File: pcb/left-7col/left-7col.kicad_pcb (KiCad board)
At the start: 2 copper layers, 126 x 92 mm, 54 parts, among them SW1 SW_SPDT_312, SW2 SW_SPST, U1 SuperMini

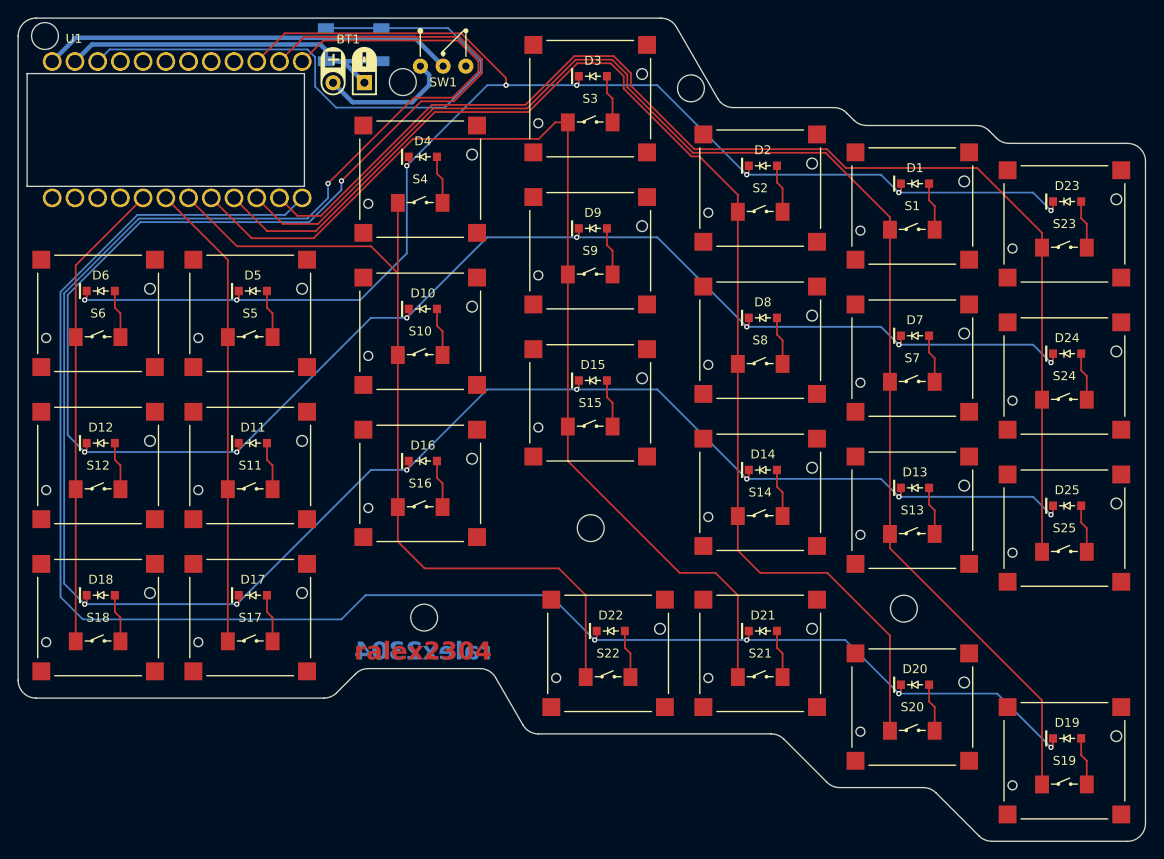
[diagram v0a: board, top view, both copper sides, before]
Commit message: Change horizontal spacing and add nice!view to left half
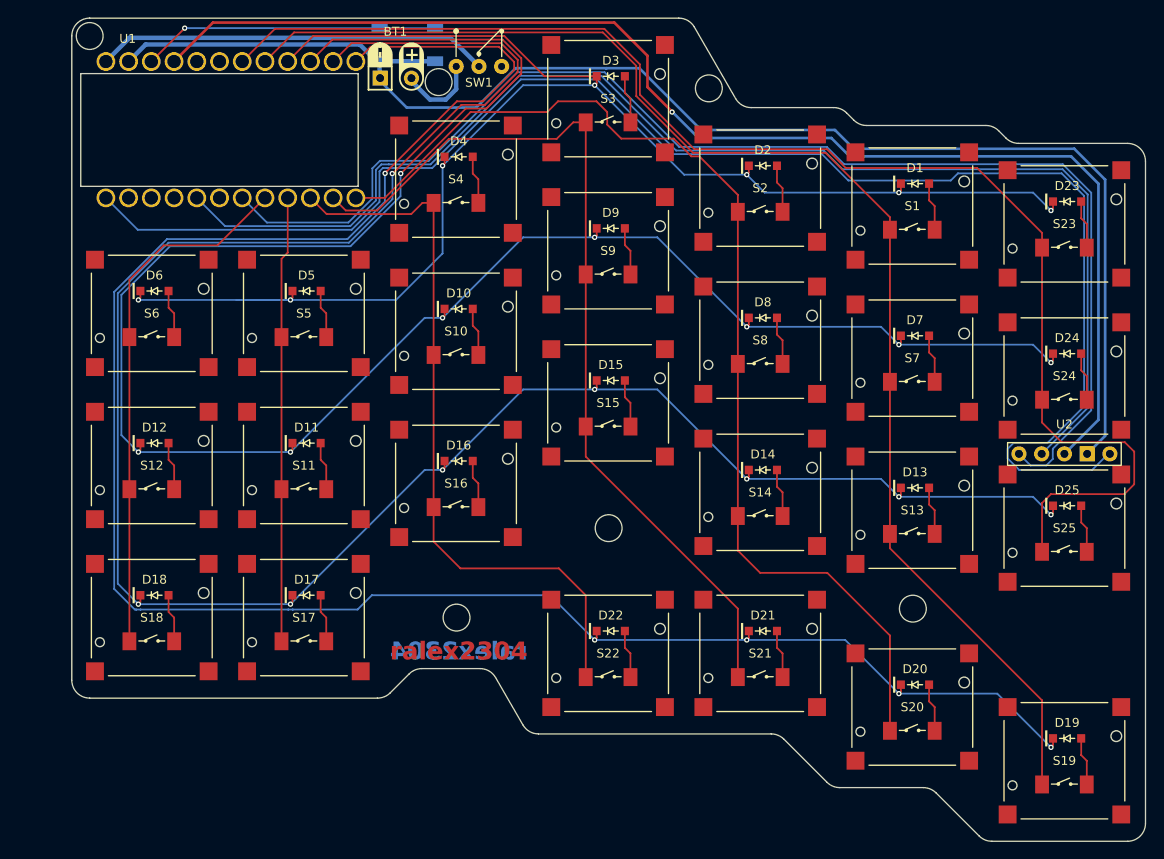
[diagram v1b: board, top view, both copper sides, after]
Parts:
- added U2: nice!view, strizh_lib:nice_view, F.Cu at (197.0, 109.0)
- moved D11 6.00 mm to (112.3, 106.5)
- moved D12 6.00 mm to (95.3, 106.5)
- moved D17 6.00 mm to (112.3, 123.5)
- moved D18 6.00 mm to (95.3, 123.5)
- moved D5 6.00 mm to (112.3, 89.5)
- moved D6 6.00 mm to (95.3, 89.5)
- moved S11 6.00 mm to (112.0, 109.0)
- moved S12 6.00 mm to (95.0, 109.0)
- moved S17 6.00 mm to (112.0, 126.0)
- moved S18 6.00 mm to (95.0, 126.0)
- moved S5 6.00 mm to (112.0, 92.0)
- moved S6 6.00 mm to (95.0, 92.0)
- moved SW2 6.00 mm to (123.6, 62.0)
- moved U1 6.00 mm to (84.8, 71.5)
- moved BT1 5.19 mm to (122.1, 64.5)
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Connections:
- U1 pad 1: unconnected-(U1-TX/D0/006-Pad1) -> cs
- U1 pad 10: COL6 -> COL3
- U1 pad 11: COL7 -> COL4
- U1 pad 12: ROW4 -> COL5
- U1 pad 13: ROW3 -> ROW4
- U1 pad 14: ROW2 -> ROW3
- U1 pad 15: ROW1 -> ROW2
- U1 pad 16: unconnected-(U1-SDA1/D13/113-Pad16) -> ROW1
- U1 pad 17: unconnected-(U1-SCL1/D14/115-Pad17) -> COL6
- U1 pad 18: unconnected-(U1-A0/D15/002-Pad18) -> COL7
- U1 pad 21: unconnected-(U1-EXT_VCC/013-Pad21) -> +3.3V
- U1 pad 5: COL1 -> sck
- U1 pad 6: COL2 -> unconnected-(U1-MISO/D3/020-Pad6)
- U1 pad 7: COL3 -> mosi
- U1 pad 8: COL4 -> COL1
- U1 pad 9: COL5 -> COL2
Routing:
- net cs: track 0.00 -> 173.6 mm
- net mosi: track 0.00 -> 146.7 mm
- net sck: track 0.00 -> 146.5 mm
- net +3.3V: track 0.00 -> 146.4 mm, vias 0 -> 1
- net -BATT: track 40.4 -> 158.8 mm
- net ROW4: track 189.8 -> 227.8 mm, vias 4 -> 5
- net rst: track 69.7 -> 33.3 mm, vias 0 -> 1
- net COL5: track 143.8 -> 123.6 mm
- net COL4: track 119.3 -> 101.9 mm
- net COL7: track 138.1 -> 155.4 mm
- net COL3: track 97.4 -> 81.5 mm
- net COL1: track 52.7 -> 59.4 mm
- net +BATT: track 15.0 -> 8.80 mm
- net ROW3: track 247.4 -> 241.3 mm
- net COL6: track 158.1 -> 152.2 mm
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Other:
- board size 126 x 92 mm -> 120 x 92 mm

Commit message: Add vias to switch footprints
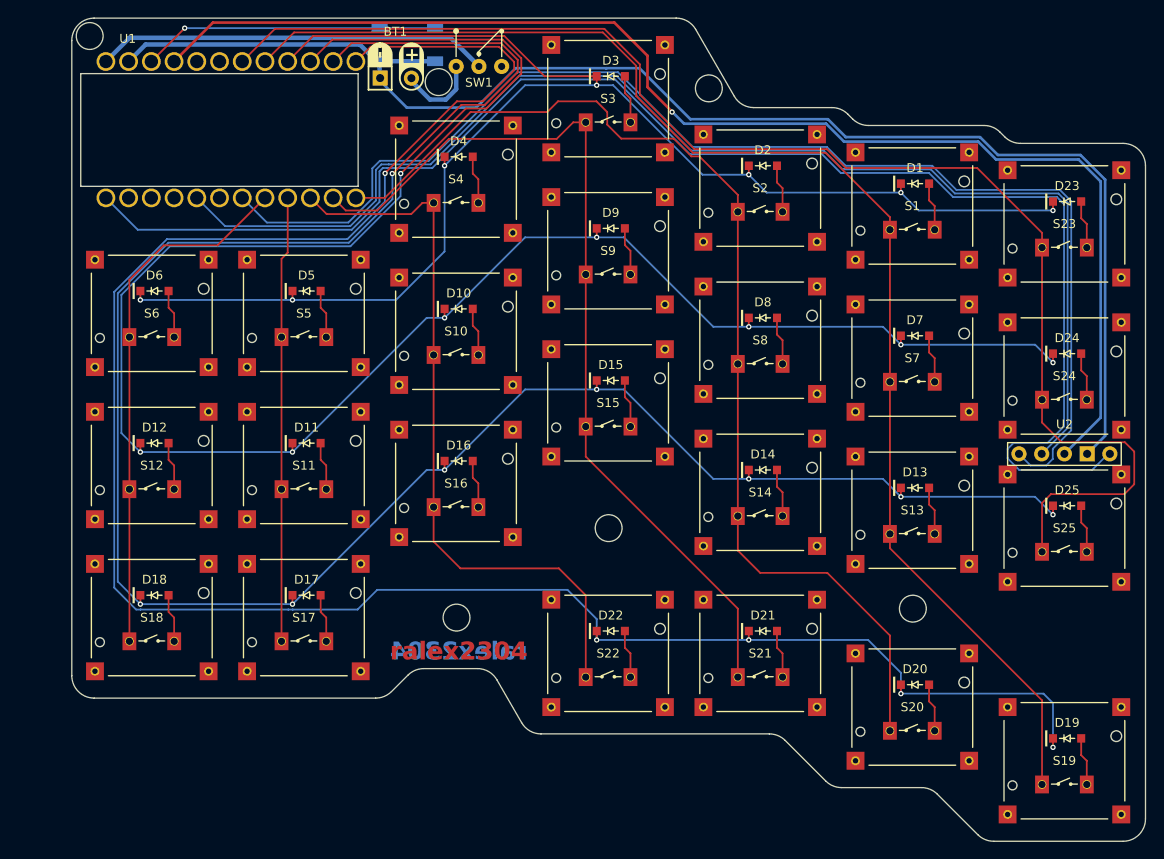
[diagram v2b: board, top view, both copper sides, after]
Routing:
- net ROW1: track 174.7 -> 167.9 mm
- net ROW4: track 227.8 -> 233.6 mm
- net cs: track 173.6 -> 169.3 mm
- net mosi: track 146.7 -> 143.0 mm
- net sck: track 146.5 -> 142.7 mm
- net ROW2: track 227.4 -> 226.8 mm
- net ROW3: track 241.3 -> 240.8 mm
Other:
- outline, holes or cut-outs redrawn

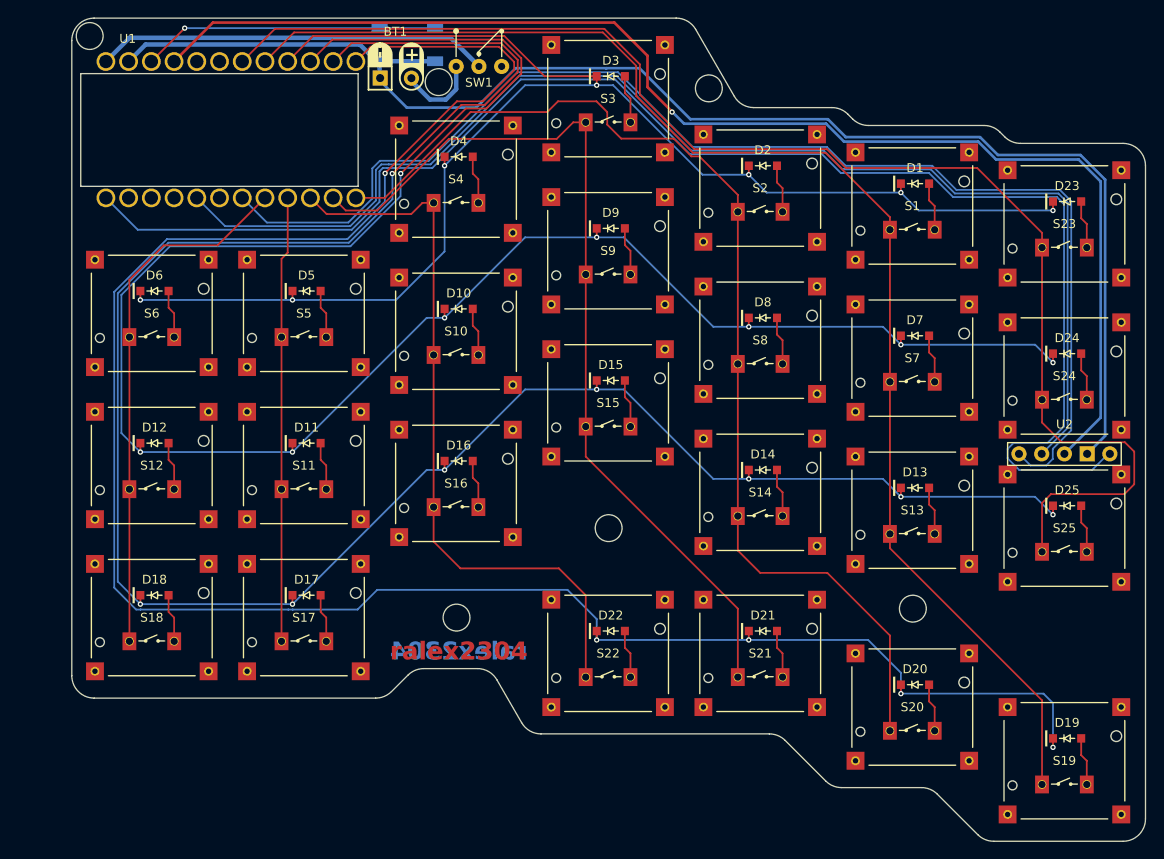
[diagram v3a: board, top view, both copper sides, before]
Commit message: Fix slight shift, enlarge vias to meet manufacturing requirements
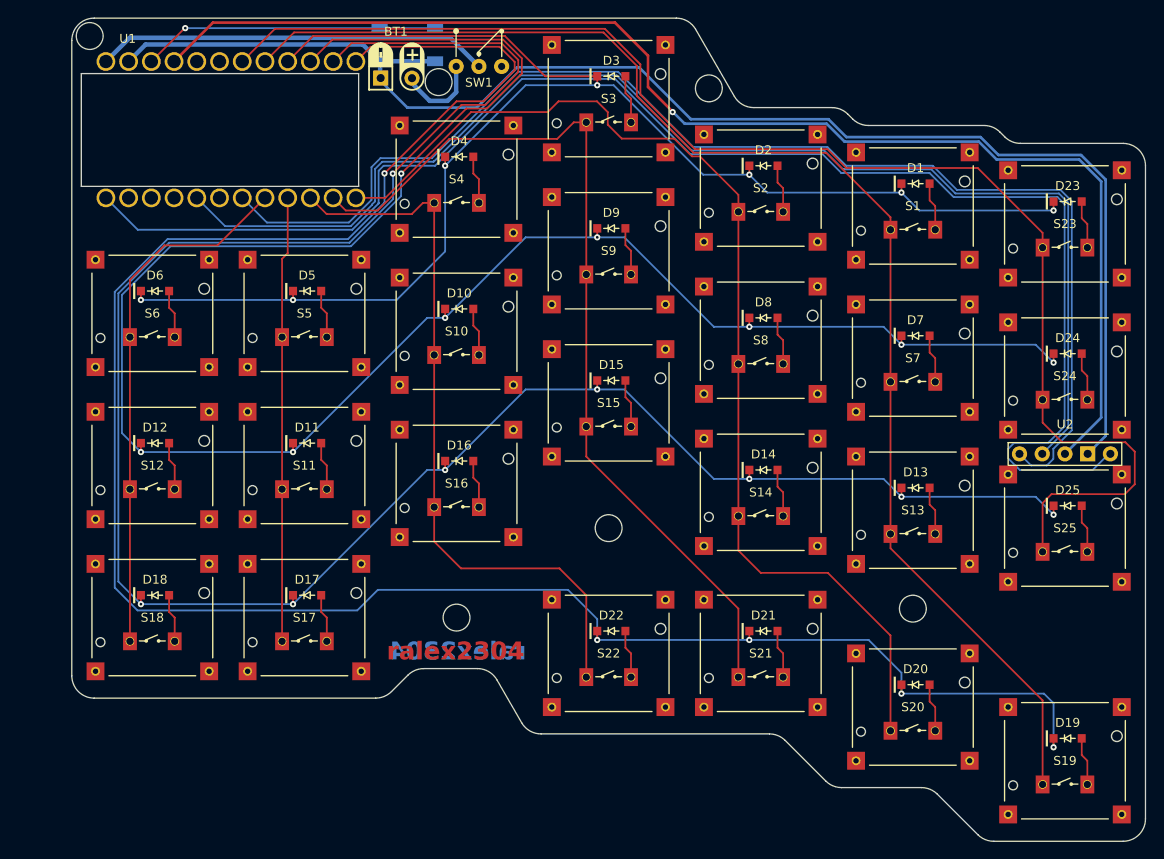
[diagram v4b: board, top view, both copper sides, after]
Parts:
- moved BT1 0.06 mm to (122.2, 64.5)
- moved D11 0.06 mm to (112.4, 106.5)
- moved D12 0.06 mm to (95.4, 106.5)
- moved D17 0.06 mm to (112.4, 123.5)
- moved D18 0.06 mm to (95.4, 123.5)
- moved D5 0.06 mm to (112.4, 89.5)
- moved D6 0.06 mm to (95.4, 89.5)
- moved S1 0.06 mm to (180.1, 80.0)
- moved S10 0.06 mm to (129.1, 94.0)
- moved S11 0.06 mm to (112.1, 109.0)
- moved S12 0.06 mm to (95.1, 109.0)
- moved S13 0.06 mm to (180.1, 114.0)
- moved S14 0.06 mm to (163.1, 112.0)
- moved S15 0.06 mm to (146.1, 102.0)
- moved S16 0.06 mm to (129.1, 111.0)
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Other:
- outline, holes or cut-outs redrawn
